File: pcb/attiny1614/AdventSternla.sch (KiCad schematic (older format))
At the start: 14 parts, among them J101 UPDI, J102 NeoPixel Data, J103 Power Out, J104 5V In, J105 GPIO_A, J106 GPIO_B, J107 GPIO_C, U101 ATTINY1614

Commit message: Corrected the diode foot print as with the power jack
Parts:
- D101: footprint Diodes_SMD:D_SOD-323 -> Diodes_SMD:D_SOD-123F
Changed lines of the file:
@@
 F 0 "D101" H 2650 3950 50  0000 C CNN
 F 1 "1N4148WSTR" H 2650 3750 50  0000 C CNN
-F 2 "Diodes_SMD:D_SOD-323" H 2650 3850 50  0001 C CNN
+F 2 "Diodes_SMD:D_SOD-123F" H 2650 3850 50  0001 C CNN
 F 3 "http://www.smc-diodes.com/propdf/1N4148WS%20N0572%20REV.B.pdf" H 2650 3850 50  0001 C CNN
 F 4 "1N4148WSTR" H 2650 3850 60  0001 C CNN "MPN"

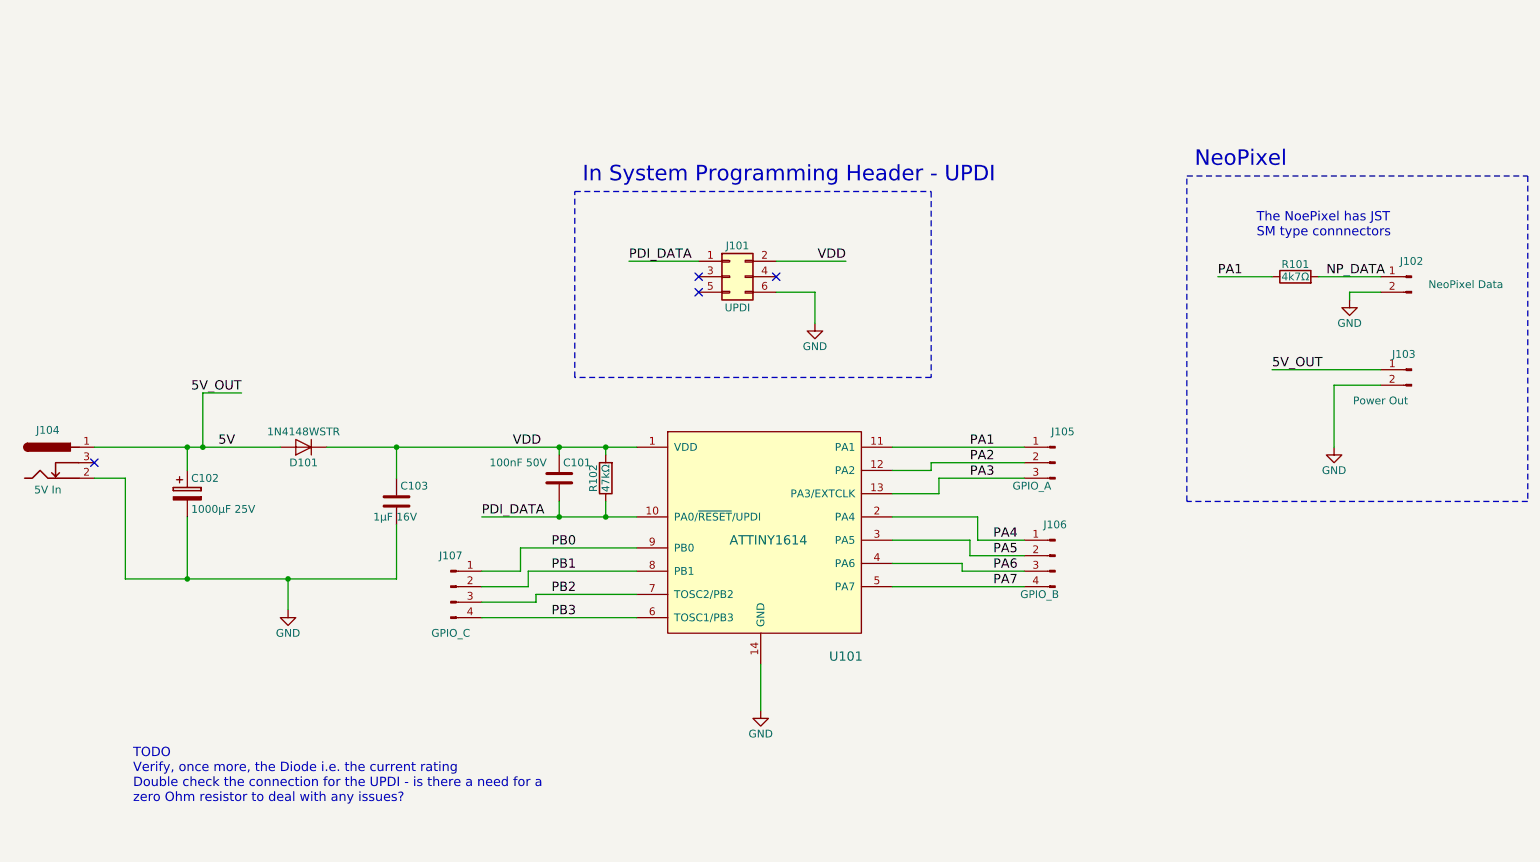
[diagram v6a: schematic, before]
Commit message: Bringing up the board - Schematic change and Clock Check Firmware
Bringing up the board, it was found that the stabilising capacitor was
not needed. A Blinky was created to verify the clock speed and work out
how to set it to the full 20MHz.
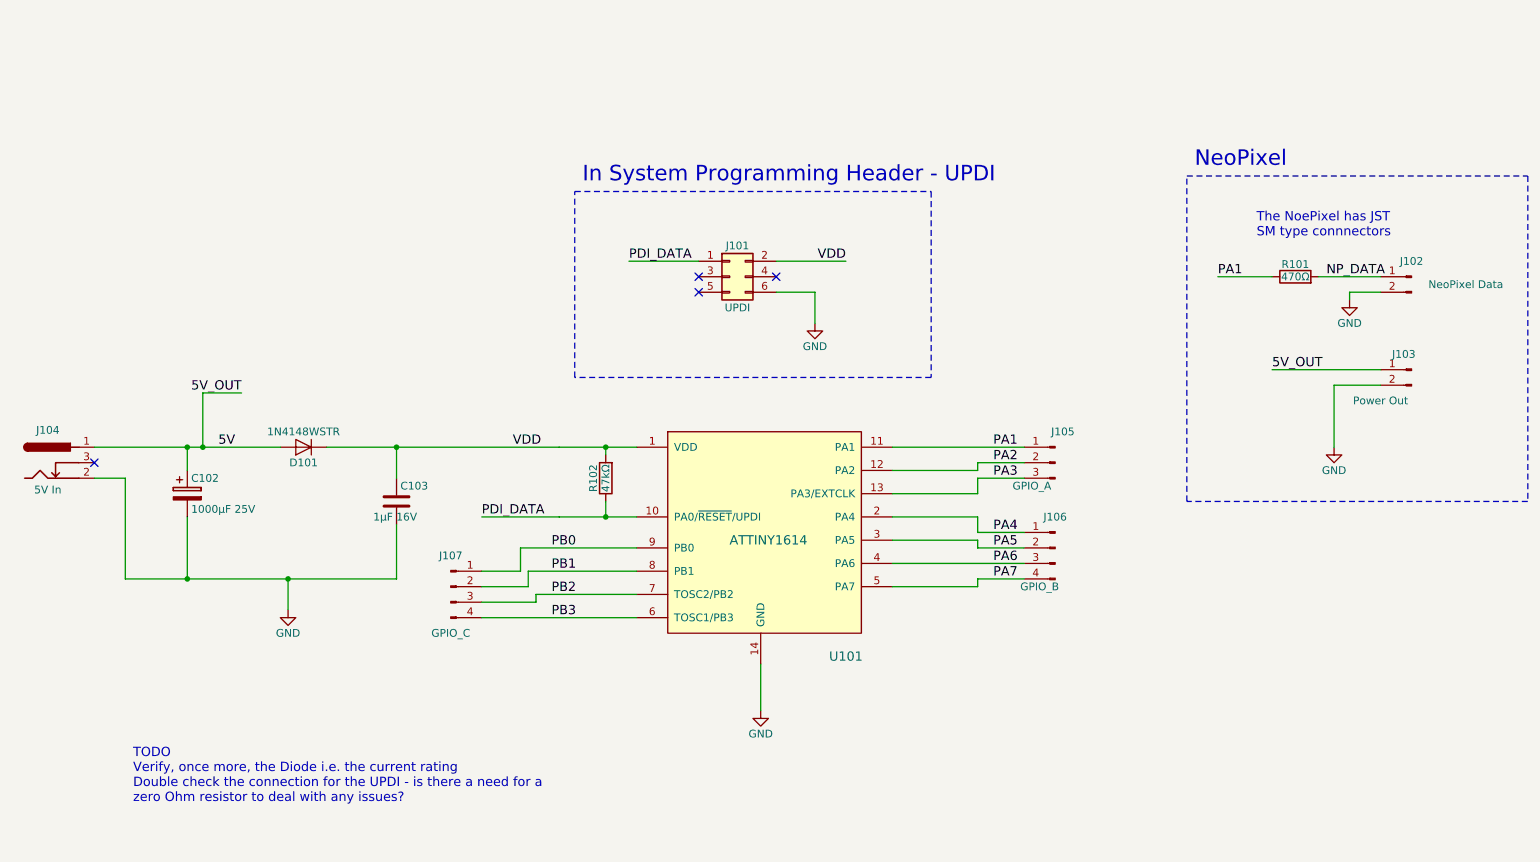
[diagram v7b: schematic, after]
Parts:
- removed C101: 100nF 50V, Capacitors_SMD:C_0805_HandSoldering, symbol C
- R101: value 4k7Ω -> 470Ω
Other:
- moved on the sheet: J106
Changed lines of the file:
@@
 NoConn ~ 5200 2850
 NoConn ~ 5700 2750
-Text Label 6950 3850 0    60   ~ 0
+Text Label 7100 3850 0    60   ~ 0
 PA1
-Text Label 6950 3950 0    60   ~ 0
+Text Label 7100 3950 0    60   ~ 0
 PA2
-Text Label 6950 4050 0    60   ~ 0
+Text Label 7100 4050 0    60   ~ 0
 PA3
-Text Label 7100 4450 0    60   ~ 0
+Text Label 7100 4400 0    60   ~ 0
 PA4
-Text Label 7100 4550 0    60   ~ 0
+Text Label 7100 4500 0    60   ~ 0
 PA5
-Text Label 7100 4650 0    60   ~ 0
+Text Label 7100 4600 0    60   ~ 0
 PA6
-Text Label 7100 4750 0    60   ~ 0
+Text Label 7100 4700 0    60   ~ 0
 PA7
 $Comp
 L Conn_01x04_Male J106
 U 1 1 59EF8DC0
-P 7500 4550
-F 0 "J106" H 7500 4750 50  0000 C CNN
-F 1 "GPIO_B" H 7600 4300 50  0000 C CNN
-F 2 "Pin_Headers:Pin_Header_Straight_1x04_Pitch2.54mm" H 7500 4550 50  0001 C CNN
-F 3 "" H 7500 4550 50  0001 C CNN
-	1    7500 4550
+P 7500 4500
+F 0 "J106" H 7500 4700 50  0000 C CNN
+F 1 "GPIO_B" H 7600 4250 50  0000 C CNN
+F 2 "Pin_Headers:Pin_Header_Straight_1x04_Pitch2.54mm" H 7500 4500 50  0001 C CNN
+F 3 "" H 7500 4500 50  0001 C CNN
+	1    7500 4500
 	-1   0    0    -1
 $EndComp
@@
 PB3
 $Comp
-L C C101
-U 1 1 59EF9591
-P 4300 4050
-F 0 "C101" H 4325 4150 50  0000 L CNN
-F 1 "100nF 50V" H 3850 4150 50  0000 L CNN
-F 2 "Capacitors_SMD:C_0805_HandSoldering" H 4338 3900 50  0001 C CNN
-F 3 "" H 4300 4050 50  0001 C CNN
-F 4 "Value" H 4300 4050 60  0001 C CNN "Link"
-	1    4300 4050
-	1    0    0    -1
-$EndComp
-$Comp
 L C C103
 U 1 1 59EF980D
@@
 P 9050 2750
 F 0 "R101" V 9130 2750 50  0000 C CNN
-F 1 "4k7Ω" V 9050 2750 50  0000 C CNN
+F 1 "470Ω" V 9050 2750 50  0000 C CNN
 F 2 "Resistors_SMD:R_0805_HandSoldering" V 8980 2750 50  0001 C CNN
 F 3 "" H 9050 2750 50  0001 C CNN
@@
 $EndComp
 Wire Wire Line
-	3800 4300 4800 4300
+	3800 4300 4300 4300
+Wire Wire Line
+	4300 4300 4600 4300
+Wire Wire Line
+	4600 4300 4800 4300
 Wire Wire Line
 	4600 4300 4600 4200
@@
 	6450 3850 7300 3850
 Wire Wire Line
-	6450 4000 6700 4000
-Wire Wire Line
-	6700 4000 6700 3950
-Wire Wire Line
-	6700 3950 7300 3950
-Wire Wire Line
-	6450 4150 6750 4150
-Wire Wire Line
-	6750 4150 6750 4050
-Wire Wire Line
-	6750 4050 7300 4050
+	6450 4000 7000 4000
+Wire Wire Line
+	7000 4000 7000 3950
+Wire Wire Line
+	7000 3950 7300 3950
+Wire Wire Line
+	6450 4150 7000 4150
+Wire Wire Line
+	7000 4150 7000 4050
+Wire Wire Line
+	7000 4050 7300 4050
 Wire Wire Line
 	6450 4300 7000 4300
 Wire Wire Line
-	6450 4450 6950 4450
-Wire Wire Line
-	6450 4600 6900 4600
-Wire Wire Line
-	6450 4750 7300 4750
-Wire Wire Line
-	1300 3850 2500 3850
+	6450 4450 7000 4450
+Wire Wire Line
+	6450 4600 7300 4600
+Wire Wire Line
+	6450 4750 7000 4750
+Wire Wire Line
+	1300 3850 1900 3850
+Wire Wire Line
+	1900 3850 2000 3850
+Wire Wire Line
+	2000 3850 2500 3850
 Wire Wire Line
 	4100 4650 4800 4650
@@
 	4800 4950 3800 4950
 Wire Wire Line
-	4300 4200 4300 4300
-Connection ~ 4300 4300
-Wire Wire Line
 	3250 3850 3250 4050
 Wire Wire Line
@@
 	4400 3400 4400 2200
 Wire Wire Line
-	6900 4600 6900 4650
-Wire Wire Line
-	6900 4650 7300 4650
-Wire Wire Line
-	6950 4450 6950 4550
-Wire Wire Line
-	6950 4550 7300 4550
-Wire Wire Line
-	7000 4300 7000 4450
-Wire Wire Line
-	7000 4450 7300 4450
+	7000 4450 7000 4500
+Wire Wire Line
+	7000 4500 7300 4500
+Wire Wire Line
+	7000 4300 7000 4400
+Wire Wire Line
+	7000 4400 7300 4400
 Wire Wire Line
 	4150 4800 4800 4800
@@
 	1900 4300 1900 4700
 Wire Wire Line
-	1500 4700 3250 4700
+	1500 4700 1900 4700
+Wire Wire Line
+	1900 4700 2550 4700
+Wire Wire Line
+	2550 4700 3250 4700
 Wire Wire Line
 	2550 4700 2550 4900
@@
 $EndComp
 Wire Wire Line
-	2800 3850 4800 3850
+	2800 3850 3250 3850
+Wire Wire Line
+	3250 3850 4300 3850
+Wire Wire Line
+	4300 3850 4600 3850
+Wire Wire Line
+	4600 3850 4800 3850
 Connection ~ 3250 3850
-Wire Wire Line
-	4300 3900 4300 3850
-Connection ~ 4300 3850
 Wire Wire Line
 	4600 3900 4600 3850
@@
 Text Notes 1550 6150 0    60   ~ 0
 TODO \nVerify, once more, the Diode i.e. the current rating\nDouble check the connection for the UPDI - is there a need for a \nzero Ohm resistor to deal with any issues?
+Wire Wire Line
+	7000 4750 7000 4700
+Wire Wire Line
+	7000 4700 7300 4700
 $EndSCHEMATC

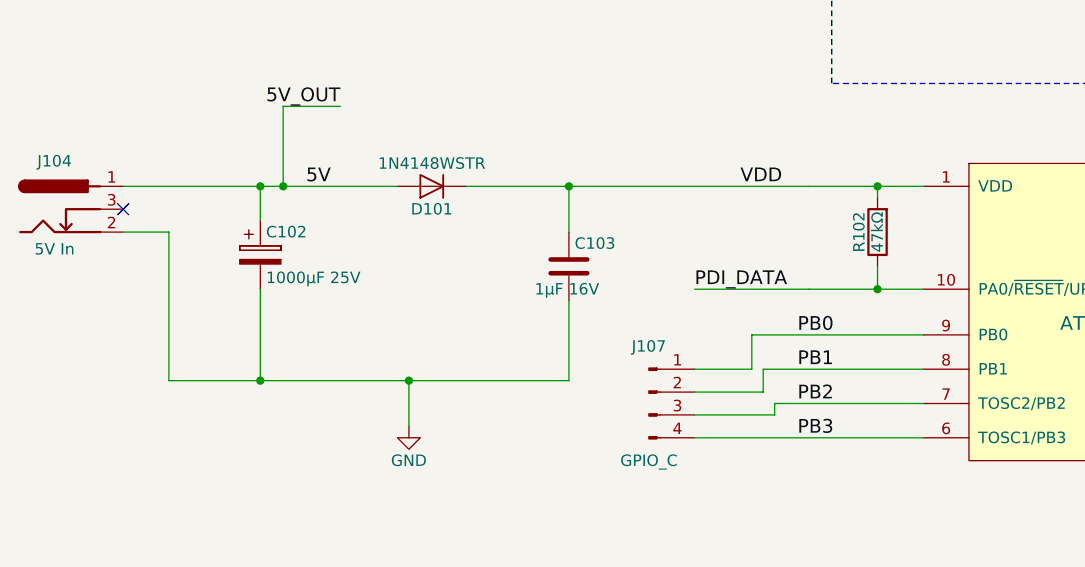
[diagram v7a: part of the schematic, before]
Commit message: Made the layout change for the unneeded C101
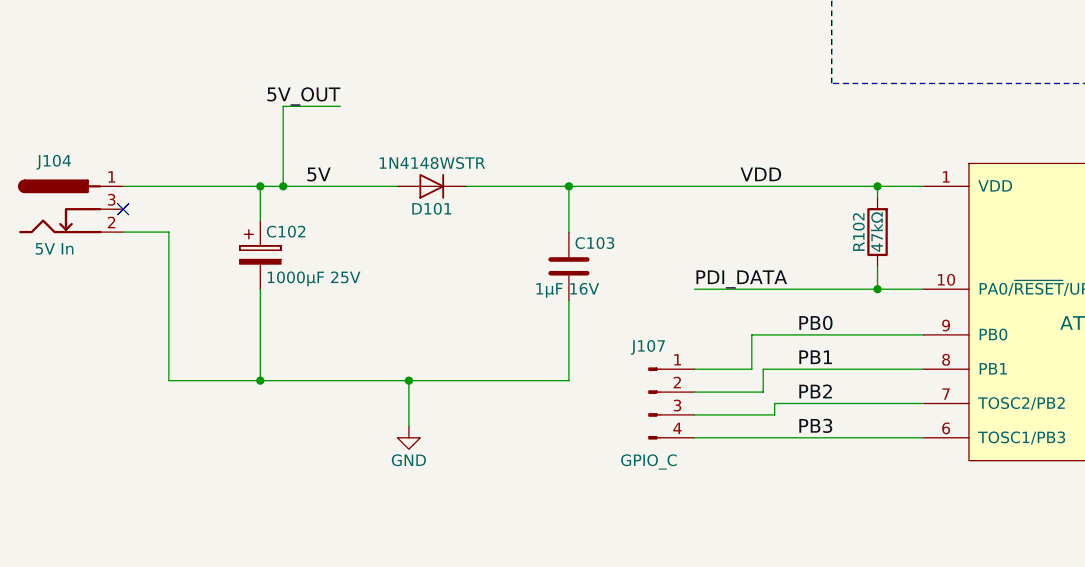
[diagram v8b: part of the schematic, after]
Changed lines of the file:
@@
 $EndComp
 Wire Wire Line
-	3800 4300 4300 4300
-Wire Wire Line
-	4300 4300 4600 4300
-Wire Wire Line
-	4600 4300 4800 4300
+	3800 4300 4800 4300
 Wire Wire Line
 	4600 4300 4600 4200
@@
 	6450 4750 7000 4750
 Wire Wire Line
-	1300 3850 1900 3850
-Wire Wire Line
-	1900 3850 2000 3850
-Wire Wire Line
-	2000 3850 2500 3850
+	1300 3850 2500 3850
 Wire Wire Line
 	4100 4650 4800 4650
@@
 	1900 4300 1900 4700
 Wire Wire Line
-	1500 4700 1900 4700
-Wire Wire Line
-	1900 4700 2550 4700
-Wire Wire Line
-	2550 4700 3250 4700
+	1500 4700 3250 4700
 Wire Wire Line
 	2550 4700 2550 4900
@@
 $EndComp
 Wire Wire Line
-	2800 3850 3250 3850
-Wire Wire Line
-	3250 3850 4300 3850
-Wire Wire Line
-	4300 3850 4600 3850
-Wire Wire Line
-	4600 3850 4800 3850
+	2800 3850 4800 3850
 Connection ~ 3250 3850
 Wire Wire Line
